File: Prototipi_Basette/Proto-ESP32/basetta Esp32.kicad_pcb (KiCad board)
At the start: 2 copper layers, 76.2 x 66 mm, 32 parts, among them J1 Conn_01x19, J2 Conn_01x19, J3 Conn_01x19, J4 Conn_01x19, J5 Screw_Terminal_01x02, J6 Conn_01x05, J7 Conn_01x02, Q1 BC547, Q2 BC547, Q3 IRF9540N, Q4 BC547, Q5 BC557, SW1 RESET, SW2 SET, U3 4013

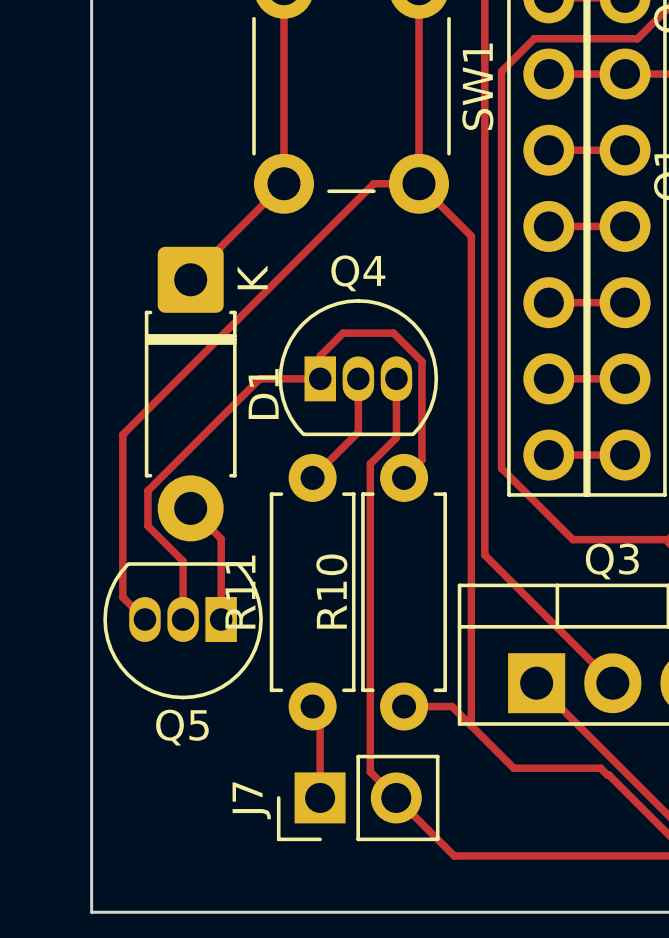
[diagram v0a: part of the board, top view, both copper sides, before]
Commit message: Versione Stabile
Versione stabile con GND a piste, senza diodo nel suicide
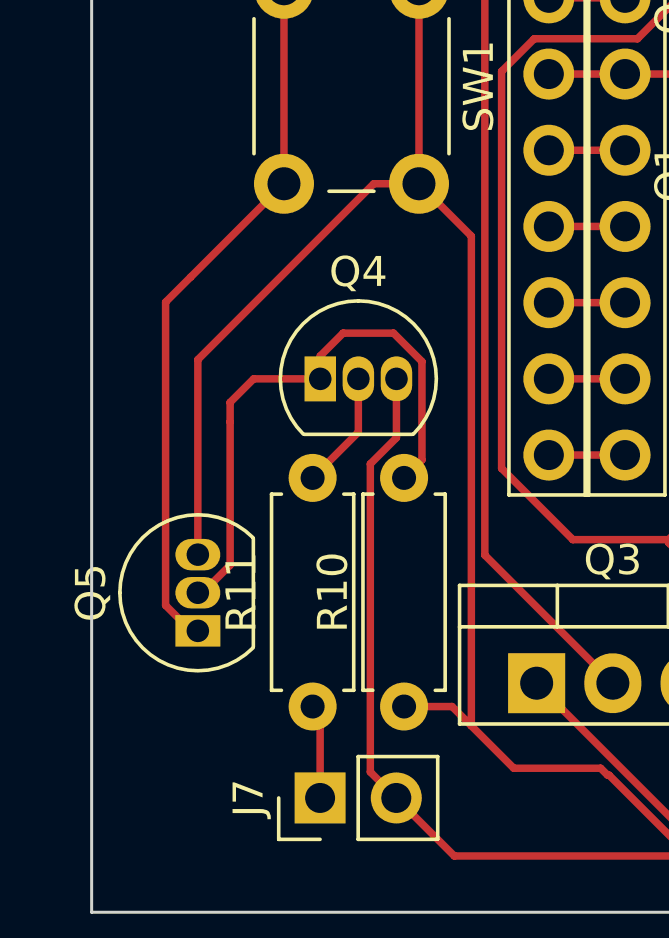
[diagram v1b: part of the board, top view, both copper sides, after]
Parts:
- removed D1: 1N4007, Diode_THT:D_DO-41_SOD81_P7.62mm_Horizontal
- moved Q5 0.86 mm to (128.0, 112.5), turned to 90 degrees
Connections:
- Q5 pad 1: Net-(D1-A) -> Suicide
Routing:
- net Suicide: track 79.9 -> 92.6 mm
- net Net-(D1-A): track 4.74 -> 0.00 mm
- net +5V: track 233.1 -> 229.6 mm
- net Net-(Q4-C): track 21.1 -> 19.2 mm

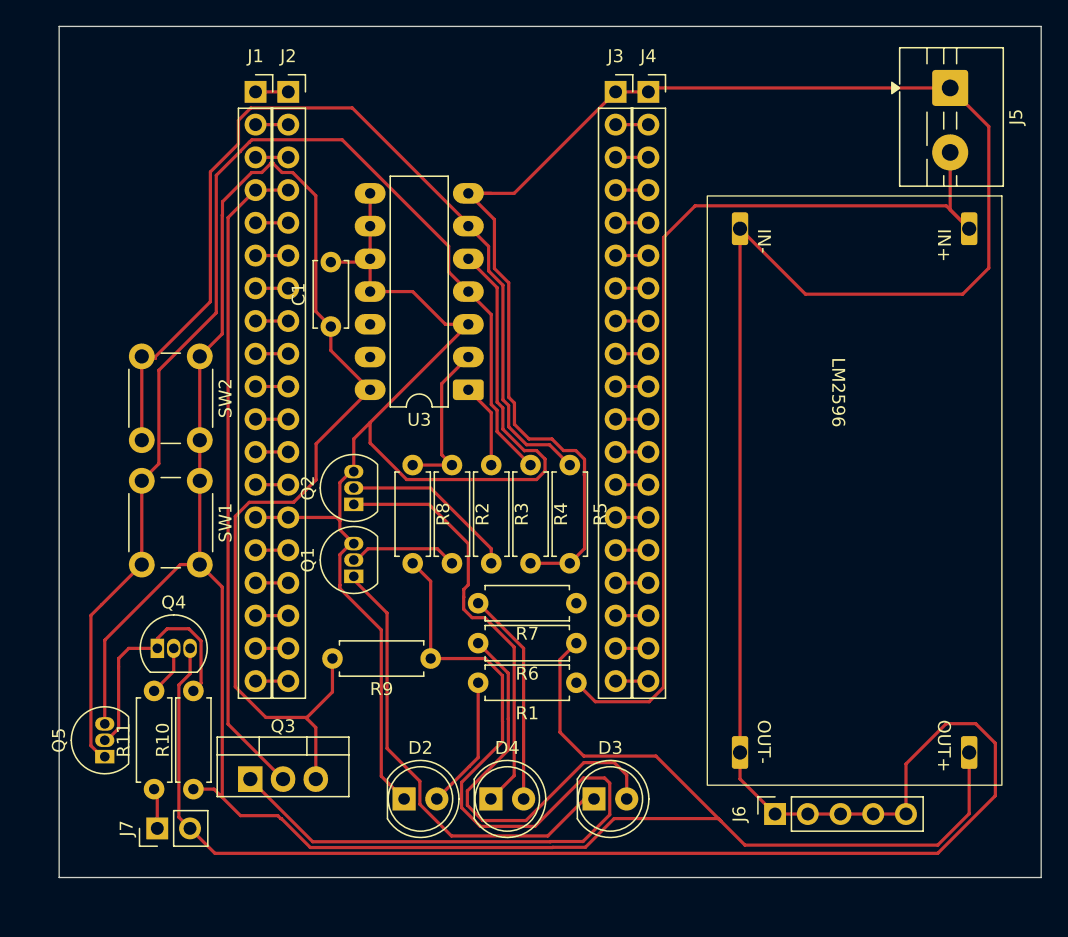
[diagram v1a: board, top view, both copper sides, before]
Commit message: Rotate TO-220 & update PCB routing
Repositioned and rotated the TO-220 footprint (added 180° orientation and updated pad AT entries), updated silk/fab outlines and UUIDs. Re-routed and widened multiple copper segments (notably +5V and V_in_Batterie nets), updated connector J1 net assignments and many segment UUIDs. Also updated project .kicad_prl accordingly.
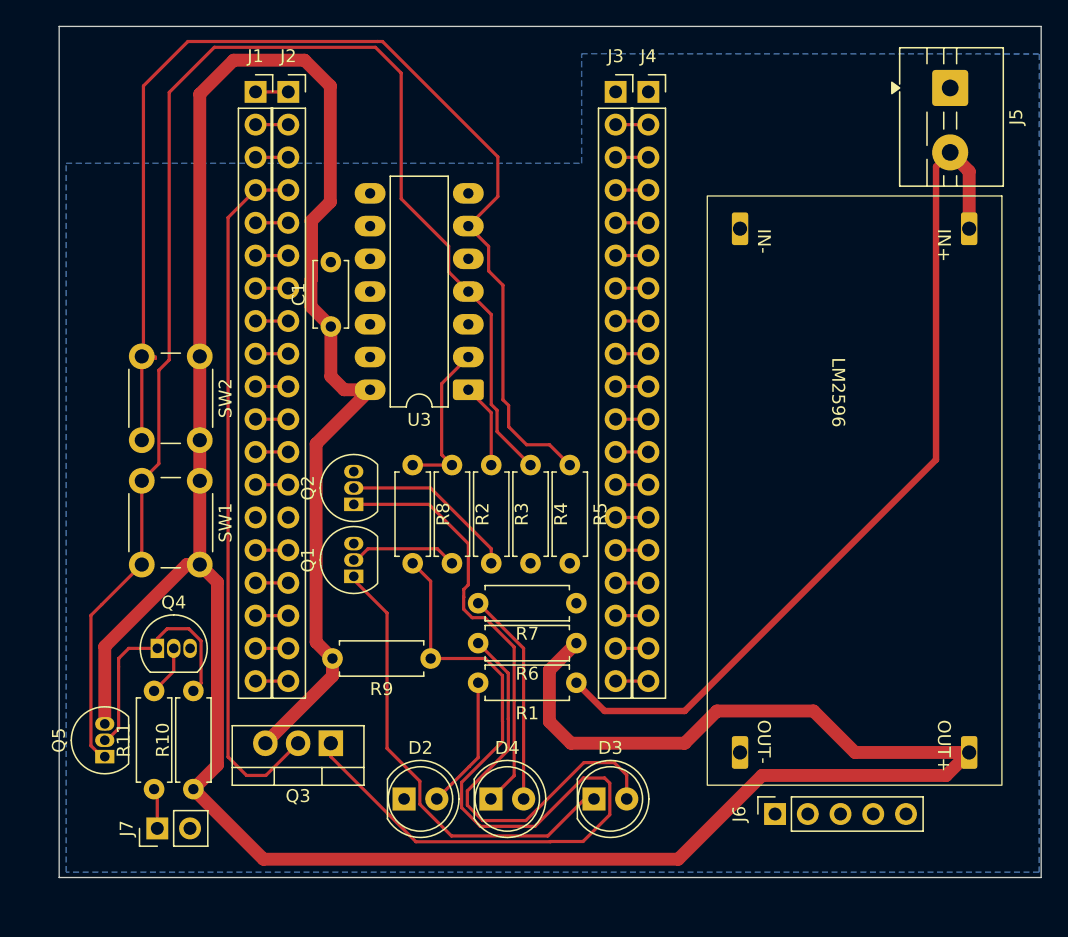
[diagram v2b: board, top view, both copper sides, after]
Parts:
- moved Q3 6.84 mm to (145.5, 111.5), turned to 180 degrees
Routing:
- net GND: track 378.6 -> 0.00 mm
- net +5V: track 229.6 -> 253.7 mm
- net Suicide: track 92.6 -> 110.1 mm
- net Net-(U3A-S): track 73.7 -> 90.6 mm
- net V_in_Batterie: track 74.7 -> 67.7 mm
- net Net-(Q3-G): track 72.6 -> 68.1 mm
- net ESP-32 POW: track 50.9 -> 54.5 mm
- added copper zone on B.Cu, net GND

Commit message: Update KiCad PCB footprint positions and metadata
Adjust PCB layout: moved and rotated multiple footprints (resistors, DIP ICs, TO-92/TO-220 transistors, push button, switch, LM2596, etc.), corrected pad orientations (added/changed pad rotation angles), and realigned reference/value text positions on F.SilkS/F.Fab. Cleaned up silkscreen/fab geometry by reordering and fixing fp_line/fp_arc coordinates and updated many element UUIDs. Also fixed a net assignment (J1 Pin 1 -> +3V3). These changes align footprints and artwork for the revised board layout and ensure pads/text orientations match the new placement.
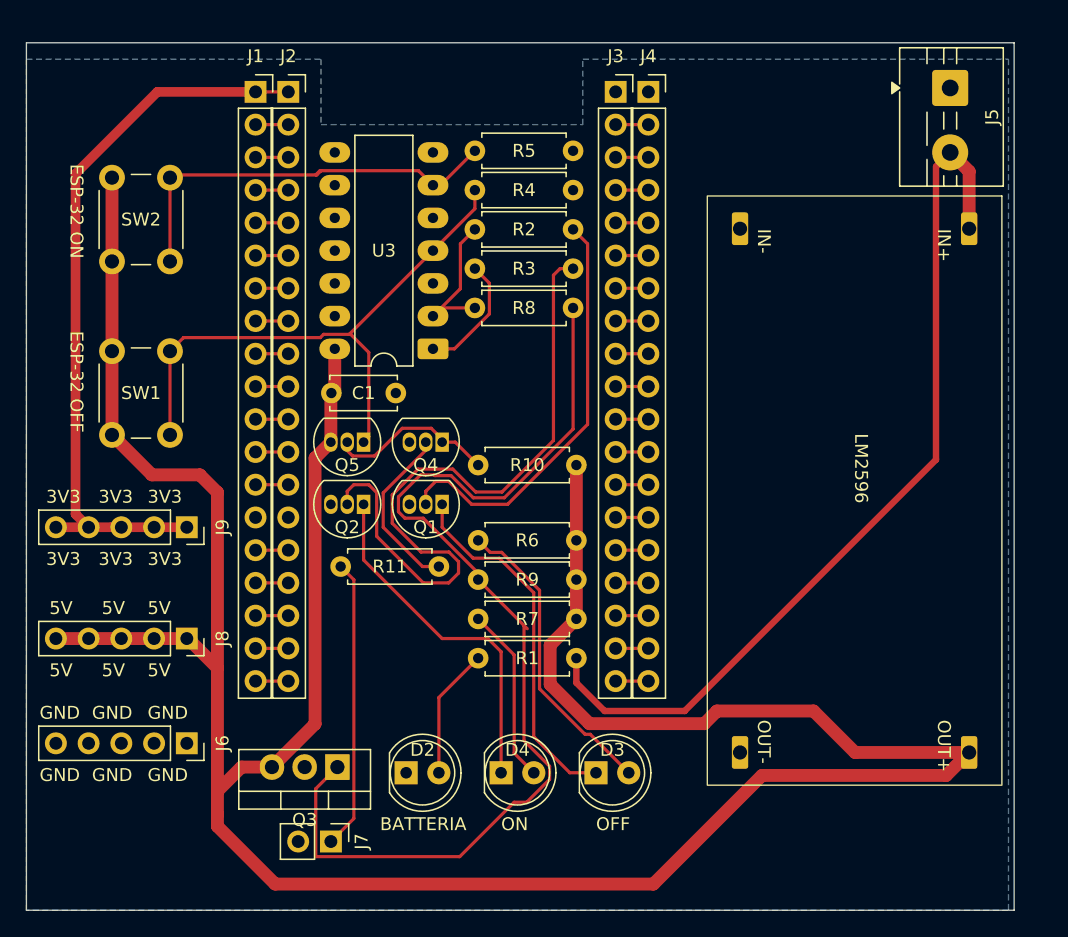
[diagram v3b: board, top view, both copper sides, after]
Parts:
- added J8: Conn_01x05, Connector_PinSocket_2.54mm:PinSocket_1x05_P2.54mm_Vertical, F.Cu at (134.4, 103.4)
- added J9: Conn_01x05, Connector_PinSocket_2.54mm:PinSocket_1x05_P2.54mm_Vertical, F.Cu at (134.4, 94.7)
- moved J6 46.0 mm to (134.4, 111.5), turned to -90 degrees
- moved R10 38.9 mm to (164.6, 89.9), turned to 180 degrees
- moved Q5 31.6 mm to (148.1, 88.1), turned to 180 degrees
- moved Q4 27.3 mm to (154.2, 88.1), turned to 180 degrees
- moved R5 25.5 mm to (156.7, 65.5), turned to 0 degrees
- moved R11 22.5 mm to (146.3, 97.8), turned to 0 degrees
- moved R4 21.8 mm to (156.7, 68.6), turned to 0 degrees
- moved R2 18.4 mm to (156.7, 71.6), turned to 0 degrees
- moved R3 15.3 mm to (156.7, 74.7), turned to 0 degrees
- moved J7 13.5 mm to (145.5, 119.1), turned to -90 degrees
- moved R8 13.1 mm to (156.7, 77.7), turned to 0 degrees
- moved SW2 10.0 mm to (128.6, 74.1), turned to 90 degrees
- moved Q1 8.85 mm to (154.2, 93.0), turned to 180 degrees
- moved R6 7.98 mm to (164.6, 95.8)
- moved SW1 7.68 mm to (128.6, 87.6), turned to 90 degrees
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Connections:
- net Net-(J1-Pin_1) renamed +3V3
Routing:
- net Suicide: track 110.1 -> 45.4 mm
- net Net-(U3A-S): track 90.6 -> 32.5 mm
- net +3V3: track 2.54 -> 57.9 mm
- net ESP-32 POW: track 54.5 -> 2.54 mm
- net Net-(Q2-B): track 13.8 -> 55.1 mm
- net +5V: track 253.7 -> 228.5 mm
- net Net-(Q1-B): track 8.81 -> 32.8 mm
- net Net-(J7-Pin_1): track 3.15 -> 22.5 mm
- net Net-(Q3-G): track 68.1 -> 82.8 mm
- net Net-(Q4-B): track 3.93 -> 13.6 mm
- net Net-(D3-A): track 31.8 -> 23.6 mm
- net Net-(D3-K): track 35.5 -> 28.2 mm
- net Net-(D4-K): track 34.1 -> 27.3 mm
- net Net-(Q4-C): track 19.2 -> 13.2 mm
- net Net-(D4-A): track 16.7 -> 13.7 mm
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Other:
- board size 76.2 x 66 mm -> 76.6 x 67.3 mm
- board text added: "3V3 3V3"
- board text added: "5V 5V"
- board text added: "BATTERIA"
- board text added: "ESP-32 OFF"
- board text added: "ESP-32 ON"
- board text added: "GND GND"
- board text added: "OFF"
- board text added: "ON"
